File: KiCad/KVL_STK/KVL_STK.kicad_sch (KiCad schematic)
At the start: 111 parts, among them SW1 SW_MEC_5G, SW10 SW_MEC_5G, SW14 SW_MEC_5G, SW15 SW_MEC_5G, SW16 SW_MEC_5G, SW17 SW_MEC_5G, SW18 SW_MEC_5G, SW19 SW_MEC_5G, SW2 SW_MEC_5G, SW20 SW_MEC_5G, SW21 SW_MEC_5G, SW22 SW_MEC_5G, SW23 SW_MEC_5G, SW27 SW_MEC_5G, SW28 SW_MEC_5G, SW29 SW_MEC_5G, SW3 SW_MEC_5G, SW30 SW_MEC_5G, SW31 SW_MEC_5G, SW32 SW_MEC_5G, SW33 SW_MEC_5G, SW34 SW_MEC_5G, SW35 SW_MEC_5G, SW36 SW_MEC_5G, SW4 SW_MEC_5G, SW41 SW_MEC_5G, SW42 SW_MEC_5G, SW44 SW_MEC_5G, SW46 SW_MEC_5G, SW47 SW_MEC_5G, SW48 SW_MEC_5G, SW49 SW_MEC_5G, SW5 SW_MEC_5G, SW6 SW_MEC_5G, SW7 SW_MEC_5G, SW8 SW_MEC_5G, SW9 SW_MEC_5G

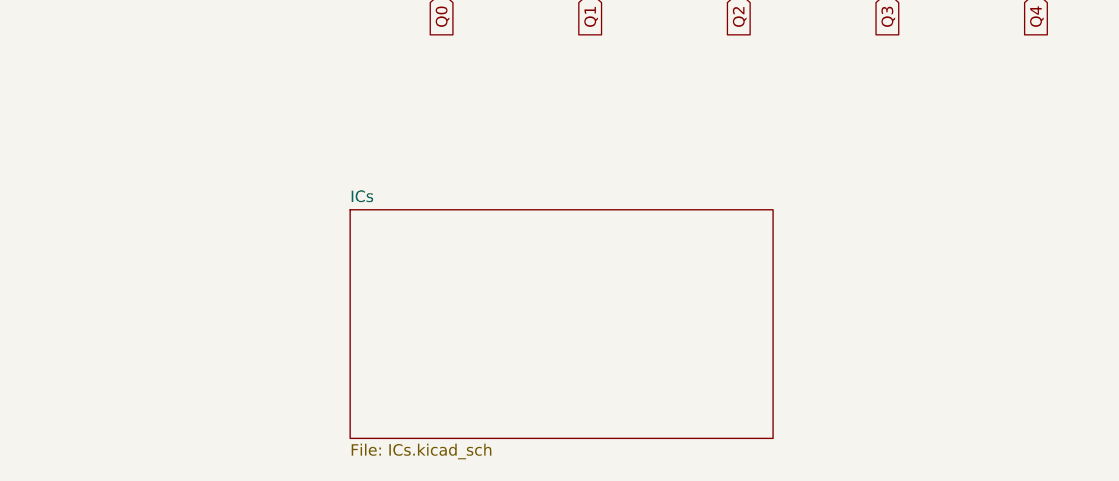
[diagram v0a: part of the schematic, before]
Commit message: Added 30 RGB LEDs.
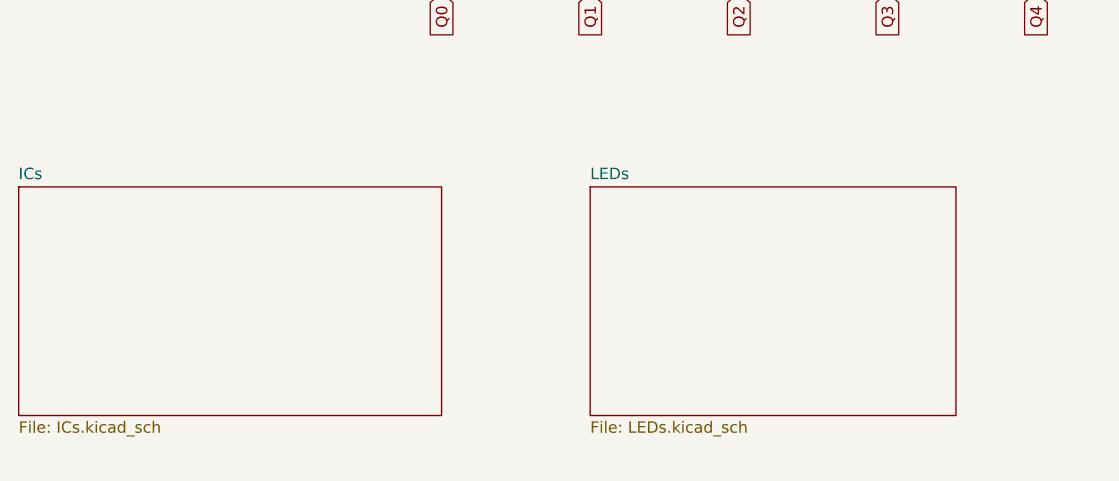
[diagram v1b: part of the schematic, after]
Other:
- added sheet LEDs (LEDs.kicad_sch)
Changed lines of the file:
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@@
 	)
 	(sheet
-		(at 62.23 165.1)
+		(at 88.9 162.56)
+		(size 40.64 25.4)
+		(fields_autoplaced yes)
+		(stroke
+			(width 0.1524)
+			(type solid)
+		)
+		(fill
+			(color 0 0 0 0.0000)
+		)
+		(property "Sheetname" "LEDs"
+			(at 88.9 161.8484 0)
+			(effects
+				(font
+					(size 1.27 1.27)
+				)
+				(justify left bottom)
+			)
+		)
+		(property "Sheetfile" "LEDs.kicad_sch"
+			(at 88.9 188.5446 0)
+			(effects
+				(font
+					(size 1.27 1.27)
+				)
+				(justify left top)
+			)
+		)
+		(instances
+			(project "KVL_STK"
+				(path "/95d3b5cf-f65f-442c-bf39-1d0330504361"
+					(page "3")
+				)
+			)
+		)
+	)
+	(sheet
+		(at 25.4 162.56)
 		(size 46.99 25.4)
 		(fields_autoplaced yes)
@@
 		)
 		(property "Sheetname" "ICs"
-			(at 62.23 164.3884 0)
+			(at 25.4 161.8484 0)
 			(effects
 				(font
@@
 		)
 		(property "Sheetfile" "ICs.kicad_sch"
-			(at 62.23 191.0846 0)
+			(at 25.4 188.5446 0)
 			(effects
 				(font
